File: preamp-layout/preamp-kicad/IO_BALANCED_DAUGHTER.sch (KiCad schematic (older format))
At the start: 55 parts, among them J82 XLR3, J83 XLR3, J84 Conn_01x03_Male, J85 Conn_01x03_Male, J86 Conn_01x03_Female, J87 Conn_01x03_Male, J88 XLR3, J89 XLR3, U21 NJM2068M, U22 NJM2068M, U23 NJM2068M

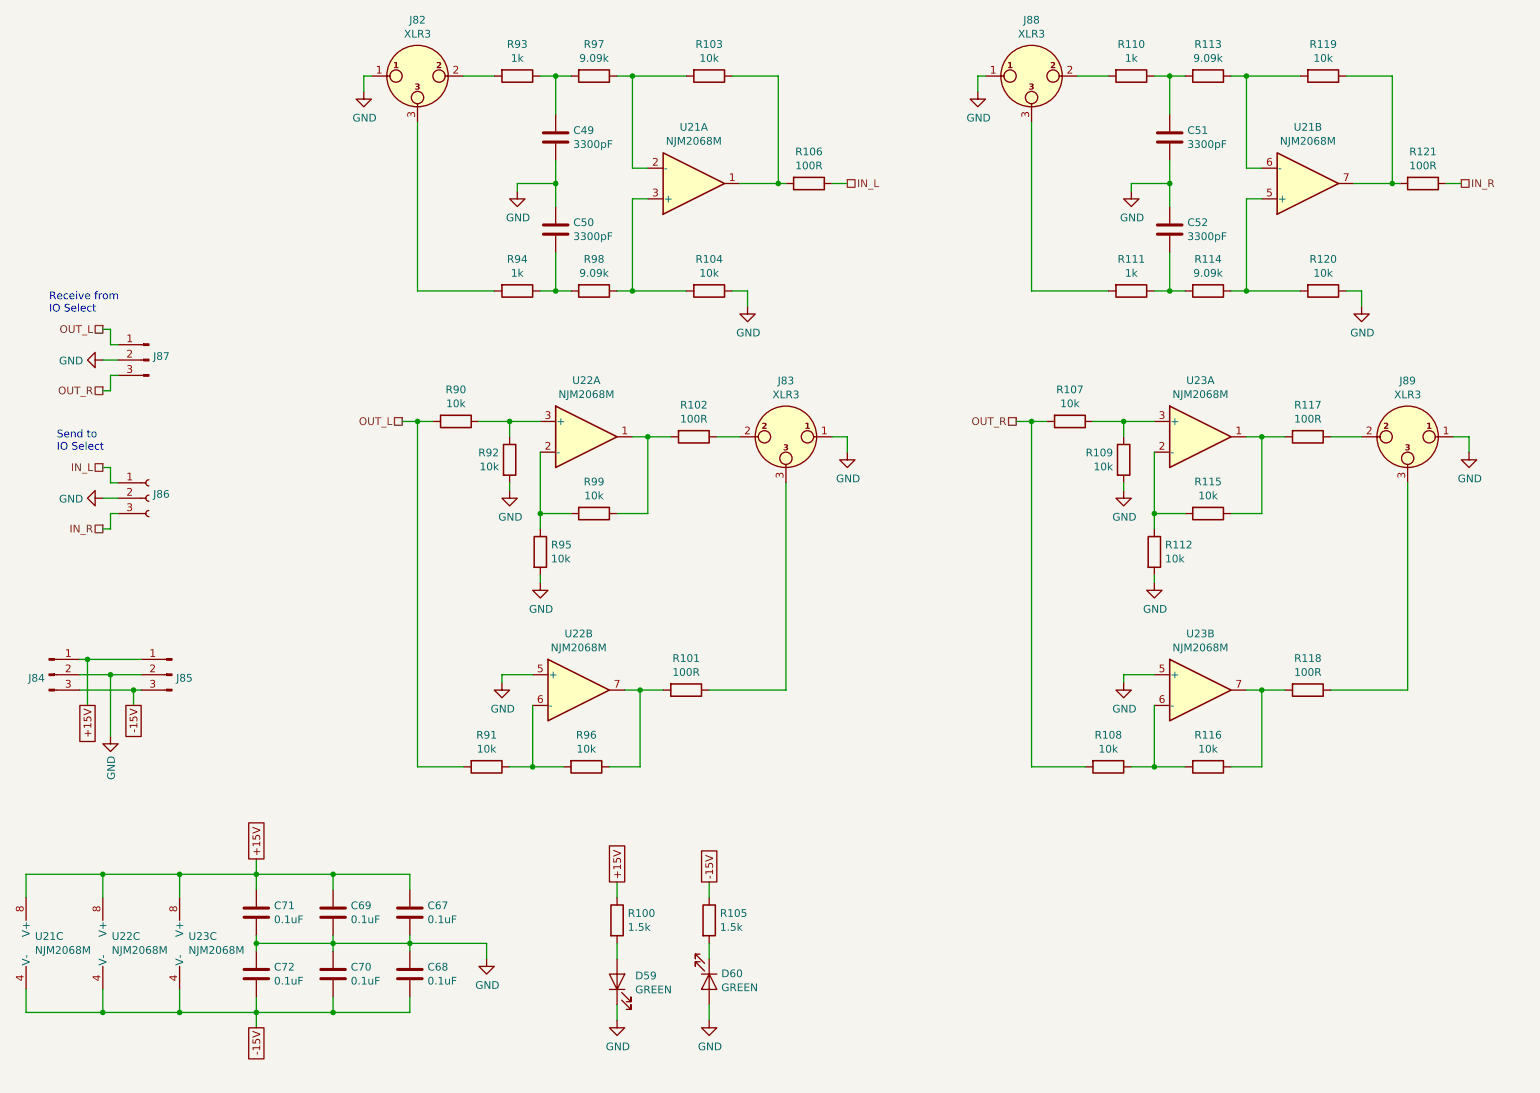
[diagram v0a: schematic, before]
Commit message: balanced IO update
other general minor updates
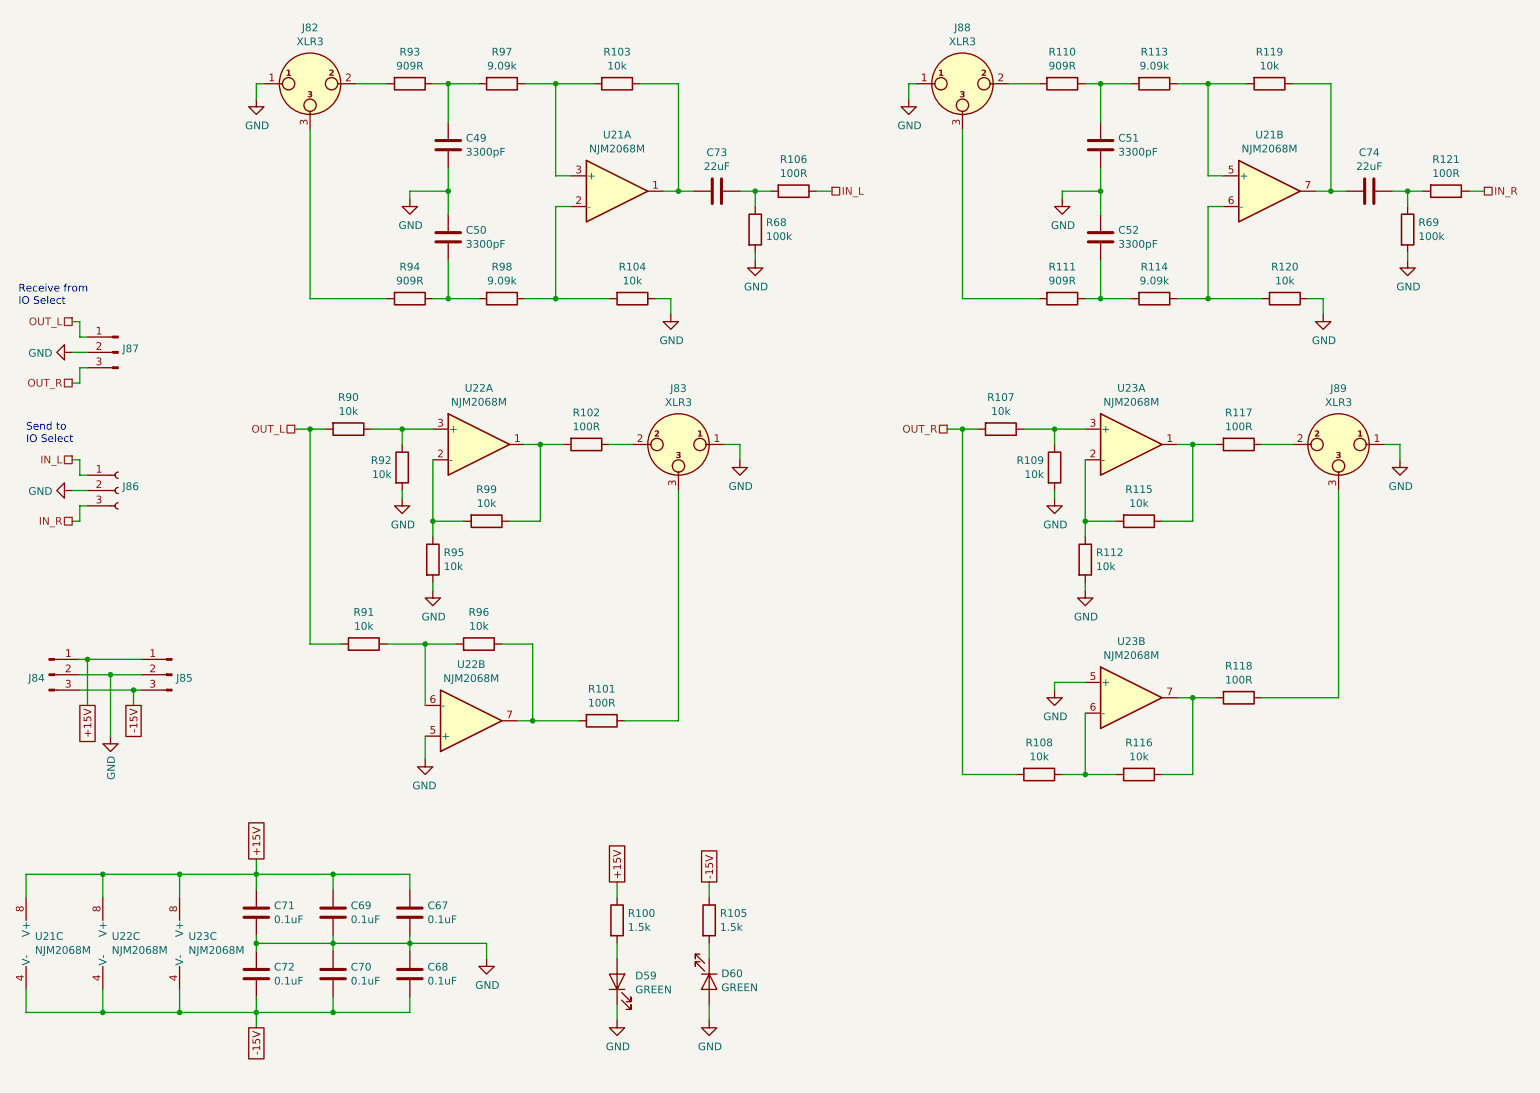
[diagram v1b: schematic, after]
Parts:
- added C73, C74: 22uF, Capacitor_SMD:C_0805_2012Metric_Pad1.15x1.40mm_HandSolder, symbol Device:C
- added R68, R69: 100k, Resistor_SMD:R_1206_3216Metric_Pad1.42x1.75mm_HandSolder, symbol Device:R
- R110, R111, R93, R94: value 1k -> 909R
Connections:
- net GND: now also R68.2, R69.2
- net at R104.2, R98.1: now also U21.2 (-); no longer U21.3 (+)
- net at R103.1, U21.1: now also C73.1; no longer R106.2
- net at R103.2, R97.1: now also U21.3 (+); no longer U21.2 (-)
- net at R114.1, R120.2: now also U21.6 (-); no longer U21.5 (+)
- net at R119.1, U21.7: now also C74.1; no longer R121.2
- net at R113.1, R119.2: now also U21.5 (+); no longer U21.6 (-)
- new net: C73.2, R106.2, R68.1
- new net: C74.2, R121.2, R69.1
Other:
- moved on the sheet: C49, C50, C51, C52, J82, J83, J86, J87, J88, J89, R101, R102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

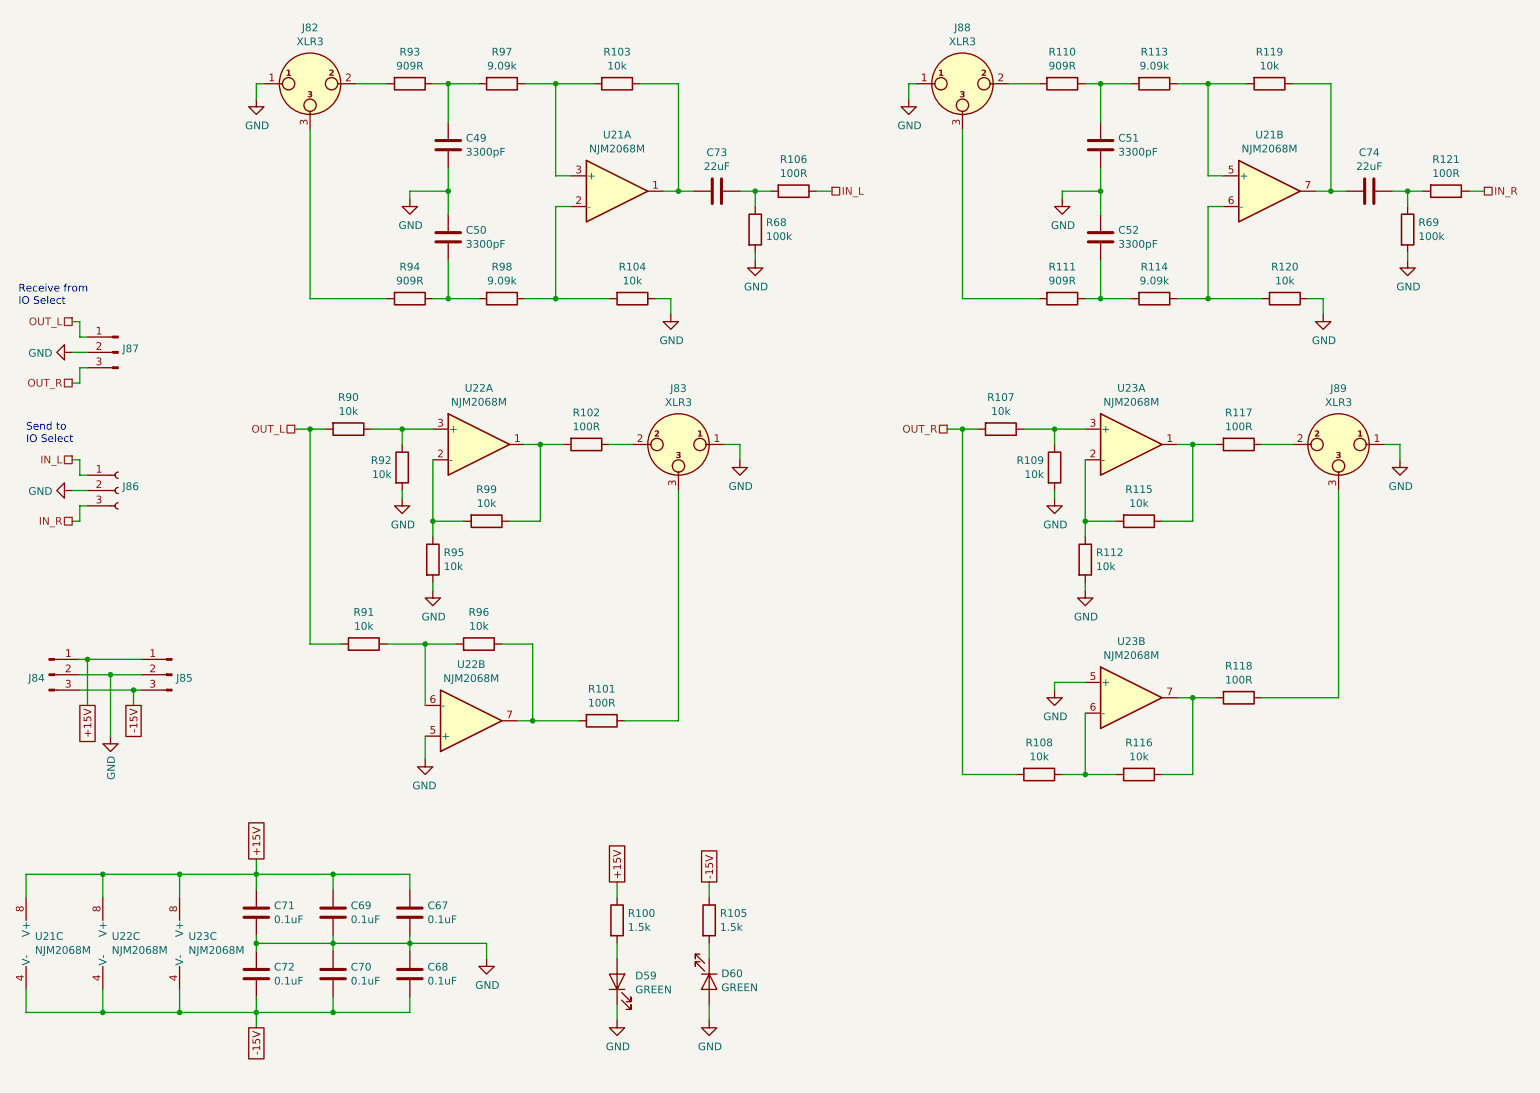
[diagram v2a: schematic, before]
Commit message: RefDes Update
Re-ran refdes assignment, updated BOM accordingly.
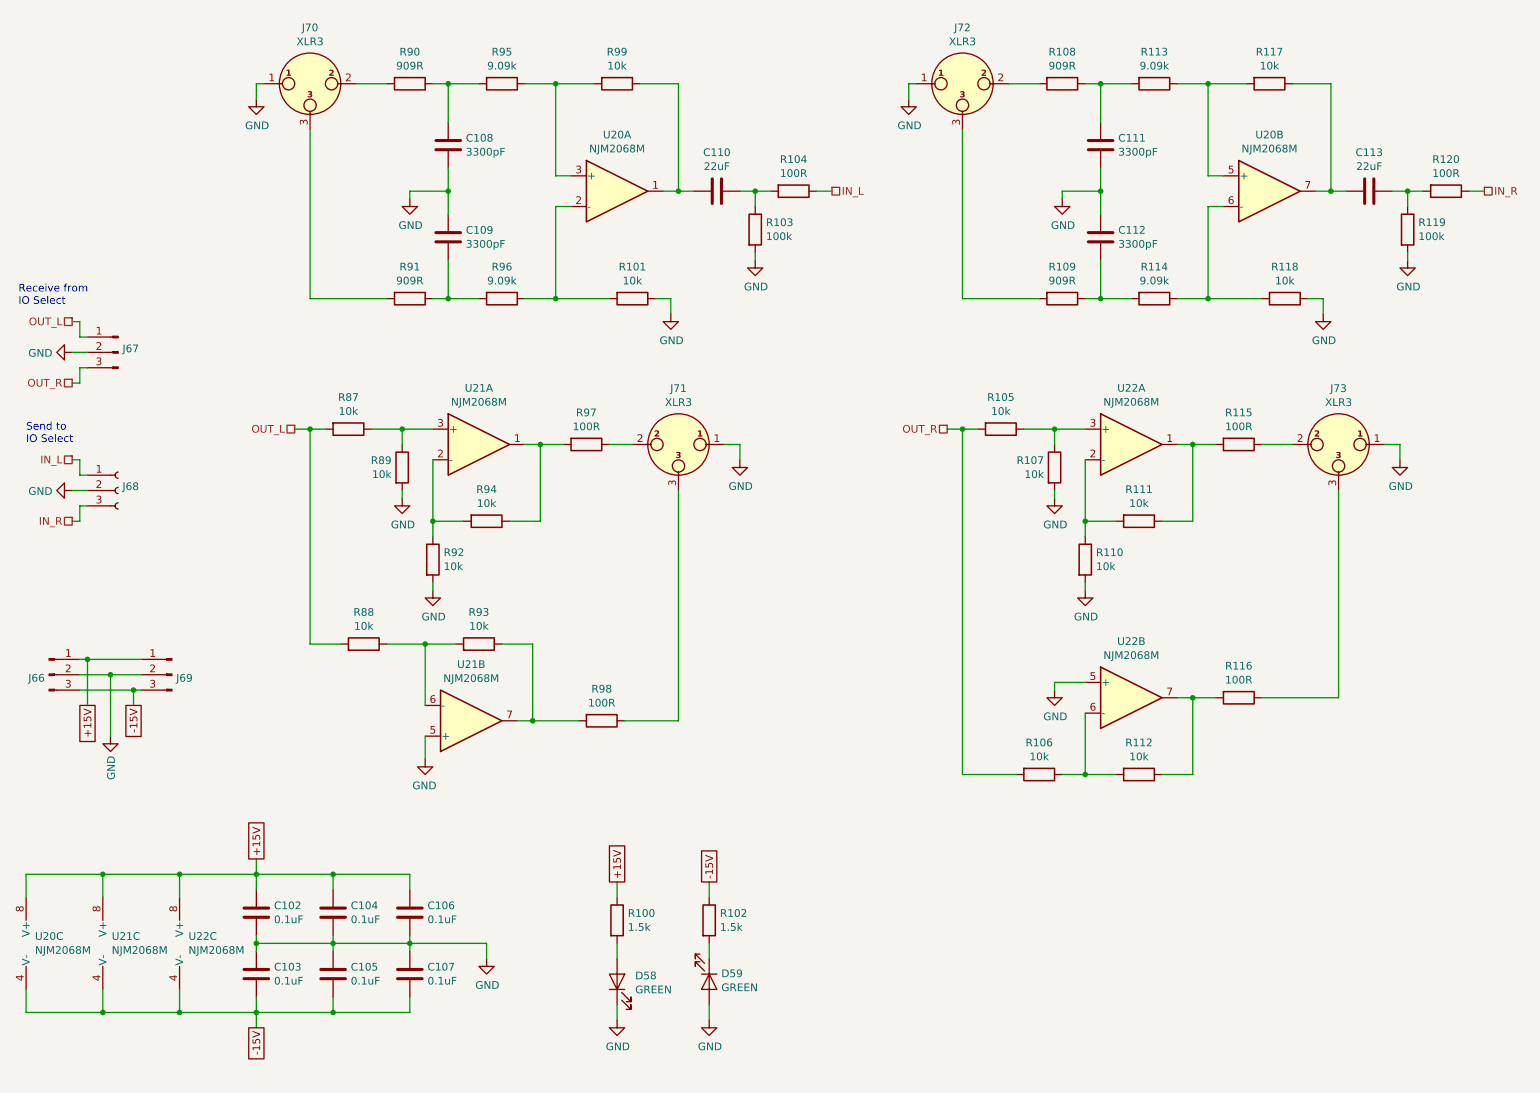
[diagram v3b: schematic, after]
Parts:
- renumbered C71 to C102, C72 to C103, C69 to C104, C70 to C105, C67 to C106, C68 to C107, C49 to C108, C50 to C109, C73 to C110, C51 to C111, C52 to C112, C74 to C113, D59 to D58, D60 to D59, J84 to J66, J87 to J67, J86 to J68, J85 to J69, J82 to J70, J83 to J71, J88 to J72, J89 to J73, R104 to R101, R105 to R102, R68 to R103, R106 to R104, R107 to R105, R108 to R106, R109 to R107, R110 to R108, R111 to R109, R112 to R110, R115 to R111, R116 to R112, R117 to R115, R118 to R116, R119 to R117, R120 to R118, R69 to R119, R121 to R120, R90 to R87, R91 to R88, R92 to R89, R93 to R90, R94 to R91, R95 to R92, R96 to R93, R99 to R94, R97 to R95, R98 to R96, R102 to R97, R101 to R98, R103 to R99, U21 to U20, U22 to U21, U23 to U22
